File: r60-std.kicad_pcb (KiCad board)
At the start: 2 copper layers, 285.8 x 95.3 mm, 170 parts, among them K0 ESC, K0A1 0, K0B1 MINUS, K0C1 EQUAL, K0D1 BACKSP, K1 1, K10 TAB, K11 Q, K12 W, K13 E, K14 R, K15 T, K16 Y, K17 U, K18 I, K19 O, K1A1 P, K1B1 LBRACE, K1C1 RBRACE, K1D1 BS_PIPE, K2 2, K20 CAPS, K20-S1 CAPS, K21 A, K22 S, K23 D, K24 F, K25 G, K26 H, K27 J, K28 K, K29 L, K2A1 COLON, K2B1 QUOTE, K2D1 ENTER, K3 3, K30 LSHIFT, K31 Z, K32 x, K33 C, K34 V, K35 B, K36 N, K37 M, K38 COMMA, K39 DOT, K3A1 SLASH, K3B1 RSHIFT, K4 4, K40 LCTL, K41 LWIN, K42 LALT, K43 LFN, K44 SSPACE-1, K45 SPACE, K45-1 SSPACE-2, K48 RALT, K49 RWIN, K4A1 RGUI, K4B1 RCTL, K5 5, K6 6, K7 7, K8 8, K9 9, P1 USB_B, SW1 SW_Push, U1 ATmega32U4-AU, Y1 16MHz

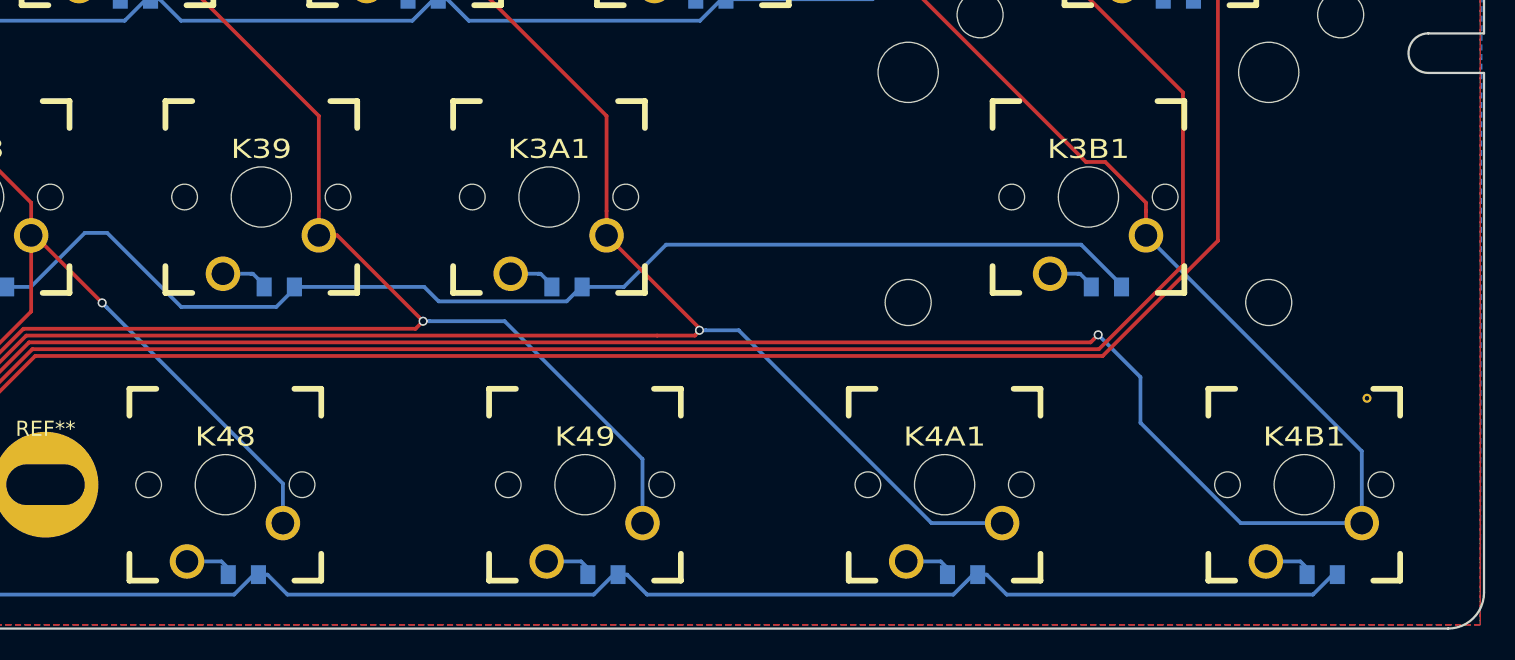
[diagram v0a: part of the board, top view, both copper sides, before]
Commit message: add option for split right shift
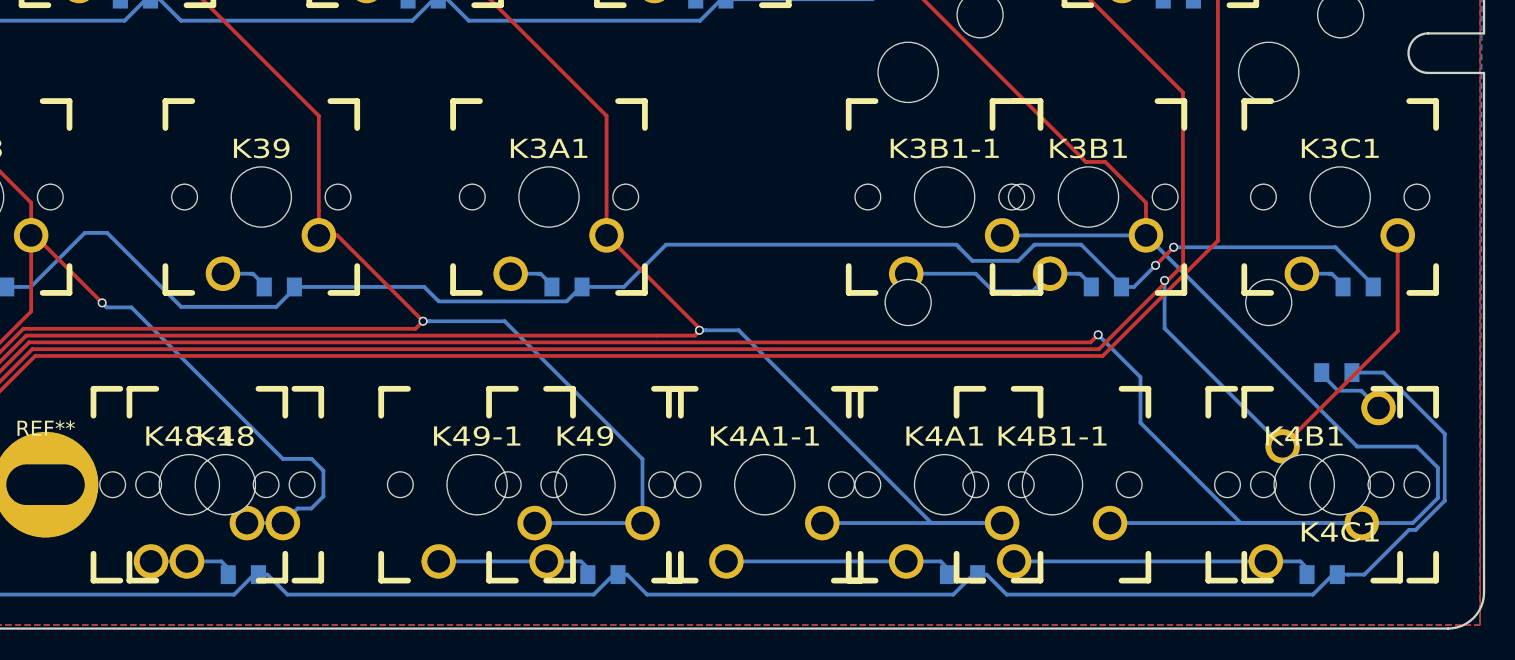
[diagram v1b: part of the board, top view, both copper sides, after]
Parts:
- removed the REF** at (306.6, 122.9)
- added D3C1: D, Keyboard:D_0805, B.Cu at (306.0, 115.5)
- added D4C1: D, Keyboard:D_0805, B.Cu at (304.6, 121.2)
- added K3B1-1: RSHIFT, Keyboard:CHERRY_PCB_175H, F.Cu at (278.6, 109.5)
- added K3C1: RFN, Keyboard:CHERRY_PCB_100H, F.Cu at (304.8, 109.5)
- added K48-1: RALT-1, Keyboard:CHERRY_PCB_100H, F.Cu at (228.6, 128.6)
- added K49-1: RWIN-1, Keyboard:CHERRY_PCB_100H, F.Cu at (247.7, 128.6)
- added K4A1-1: RGUI-1, Keyboard:CHERRY_PCB_100H, F.Cu at (266.7, 128.6)
- added K4B1-1: RCTL-1, Keyboard:CHERRY_PCB_100H, F.Cu at (285.8, 128.6)
- added K4C1: RFN, Keyboard:CHERRY_PCB_100H, F.Cu at (304.8, 128.6)
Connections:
- U1 pad 1: (no net) -> Net-(U1-Pad1)
- U1 pad 25: (no net) -> Net-(U1-Pad25)
- U1 pad 32: (no net) -> Net-(U1-Pad32)
- U1 pad 8: (no net) -> Net-(U1-Pad8)
- U1 pad 9: (no net) -> Net-(U1-Pad9)
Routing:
- net /C11: track 242.2 -> 276.9 mm
- net /C12: track 190.2 -> 221.9 mm, vias 1 -> 2
- net /R4: track 314.4 -> 335.8 mm
- net /R3: track 334.8 -> 354.6 mm, vias 4 -> 6
- net Net-(D4B1-Pad2): track 3.32 -> 20.0 mm
- net Net-(D4A1-Pad2): track 3.32 -> 15.2 mm
- net /C10: track 188.4 -> 200.3 mm
- net Net-(D3B1-Pad2): track 3.17 -> 13.6 mm
- net /C8: track 140.5 -> 147.7 mm
- net Net-(D49-Pad2): track 3.32 -> 10.5 mm
- net /C9: track 167.5 -> 174.7 mm
- net Net-(D4C1-Pad2): track 0.00 -> 4.81 mm
- net Net-(D3C1-Pad2): track 0.00 -> 3.17 mm
- net Net-(D48-Pad2): track 3.32 -> 5.70 mm
